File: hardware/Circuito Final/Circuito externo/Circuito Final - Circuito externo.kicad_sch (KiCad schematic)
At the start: 67 parts, among them J1 Conn_02x19_Odd_Even, J2 Conn_02x19_Odd_Even, J3 Conn_01x02, J4 Conn_01x02, J5 Conn_01x03_Pin, Q1 FDMS6681Z, Q2 FDMS6681Z, Q3 MMBT2222A, SW1 SW_SPDT, SW2 SW_DIP_x04, SW3 SW_DIP_x04, SW4 SW_DIP_x01, SW5 SW_DIP_x01, SW6 SW_DIP_x01, U1 Opamp_Quad, U2 ICL7660, U3 INA180A1

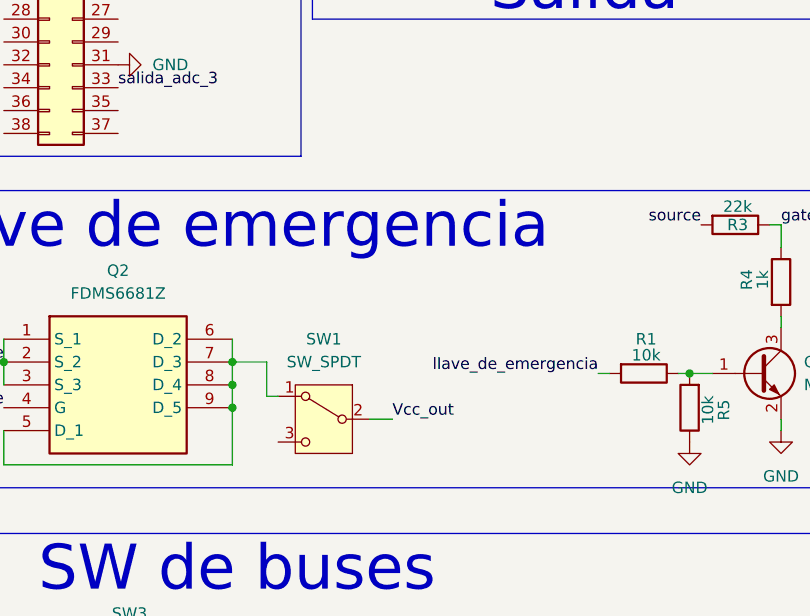
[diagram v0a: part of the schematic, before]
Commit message: agrega pull down en llave de emergencia
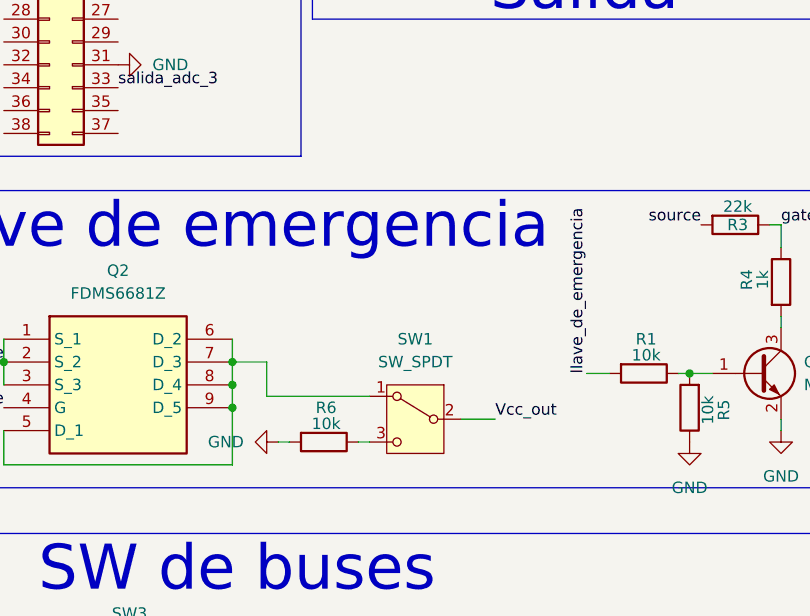
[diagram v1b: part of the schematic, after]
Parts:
- added R6: 10k, Resistor_SMD:R_1206_3216Metric_Pad1.30x1.75mm_HandSolder, symbol Device:R
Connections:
- net GND: now also R6.2
- net at SW1.3 (C): now also R6.1
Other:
- moved on the sheet: SW1
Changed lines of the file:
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@@
 	(wire
 		(pts
-			(xy 102.87 113.03) (xy 105.41 113.03)
-		)
-		(stroke
-			(width 0)
-			(type default)
-		)
-	)
-	(wire
-		(pts
 			(xy 138.43 107.95) (xy 140.97 107.95)
 		)
@@
 	(wire
 		(pts
+			(xy 93.98 115.57) (xy 92.71 115.57)
+		)
+		(stroke
+			(width 0)
+			(type default)
+		)
+	)
+	(wire
+		(pts
 			(xy 251.46 120.65) (xy 248.92 120.65)
 		)
@@
 	(wire
 		(pts
-			(xy 128.27 107.95) (xy 129.54 107.95)
+			(xy 127 107.95) (xy 129.54 107.95)
 		)
 		(stroke
@@
 	(wire
 		(pts
+			(xy 102.87 115.57) (xy 101.6 115.57)
+		)
+		(stroke
+			(width 0)
+			(type default)
+		)
+	)
+	(wire
+		(pts
 			(xy 208.28 55.88) (xy 213.36 55.88)
 		)
@@
 	(wire
 		(pts
+			(xy 113.03 113.03) (xy 116.84 113.03)
+		)
+		(stroke
+			(width 0)
+			(type default)
+		)
+	)
+	(wire
+		(pts
 			(xy 62.23 104.14) (xy 62.23 106.68)
 		)
@@
 	(wire
 		(pts
-			(xy 91.44 110.49) (xy 92.71 110.49)
+			(xy 91.44 110.49) (xy 102.87 110.49)
 		)
 		(stroke
@@
 	)
 	(label "Vcc_out"
-		(at 105.41 113.03 0)
+		(at 116.84 113.03 0)
 		(effects
 			(font
@@
 	)
 	(label "llave_de_emergencia"
-		(at 128.27 107.95 180)
+		(at 127 107.95 90)
 		(effects
 			(font
 				(size 1.27 1.27)
 			)
-			(justify right bottom)
+			(justify left bottom)
 		)
 	)
@@
 	)
 	(symbol
+		(lib_id "Device:R")
+		(at 97.79 115.57 270)
+		(unit 1)
+		(body_style 1)
+		(exclude_from_sim no)
+		(in_bom yes)
+		(on_board yes)
+		(in_pos_files yes)
+		(dnp no)
+		(property "Reference" "R6"
+			(at 98.044 111.76 90)
+			(show_name no)
+			(do_not_autoplace no)
+			(effects
+				(font
+					(size 1.27 1.27)
+				)
+			)
+		)
+		(property "Value" "10k"
+			(at 98.044 113.538 90)
+			(show_name no)
+			(do_not_autoplace no)
+			(effects
+				(font
+					(size 1.27 1.27)
+				)
+			)
+		)
+		(property "Footprint" "Resistor_SMD:R_1206_3216Metric_Pad1.30x1.75mm_HandSolder"
+			(at 97.79 113.792 90)
+			(hide yes)
+			(show_name no)
+			(do_not_autoplace no)
+			(effects
+				(font
+					(size 1.27 1.27)
+				)
+			)
+		)
+		(property "Datasheet" ""
+			(at 97.79 115.57 0)
+			(hide yes)
+			(show_name no)
+			(do_not_autoplace no)
+			(effects
+				(font
+					(size 1.27 1.27)
+				)
+			)
+		)
+		(property "Description" "Resistor"
+			(at 97.79 115.57 0)
+			(hide yes)
+			(show_name no)
+			(do_not_autoplace no)
+			(effects
+				(font
+					(size 1.27 1.27)
+				)
+			)
+		)
+		(pin "1"
+		)
+		(pin "2"
+		)
+		(instances
+			(project "Circuito Final - Circuito externo"
+				(path "/f0782466-24b0-4466-90f1-cde2f15c75b0"
+					(reference "R6")
+					(unit 1)
+				)
+			)
+		)
+	)
+	(symbol
 		(lib_id "Connector_Generic:Conn_02x07_Odd_Even")
 		(at 34.29 182.88 0)
@@
 	(symbol
 		(lib_id "Switch:SW_SPDT")
-		(at 97.79 113.03 0)
+		(at 107.95 113.03 0)
 		(mirror y)
 		(unit 1)
@@
 		(fields_autoplaced yes)
 		(property "Reference" "SW1"
-			(at 97.79 104.14 0)
+			(at 107.95 104.14 0)
 			(show_name no)
 			(do_not_autoplace no)
@@
 		)
 		(property "Value" "SW_SPDT"
-			(at 97.79 106.68 0)
+			(at 107.95 106.68 0)
 			(show_name no)
 			(do_not_autoplace no)
@@
 		)
 		(property "Footprint" "Button_Switch_THT:SW_Slide_SPDT_Straight_CK_OS102011MS2Q"
-			(at 97.79 113.03 0)
+			(at 107.95 113.03 0)
 			(hide yes)
 			(show_name no)
@@
 		)
 		(property "Datasheet" ""
-			(at 97.79 120.65 0)
+			(at 107.95 120.65 0)
 			(hide yes)
 			(show_name no)
@@
 		)
 		(property "Description" "Switch, single pole double throw"
-			(at 97.79 113.03 0)
+			(at 107.95 113.03 0)
 			(hide yes)
 			(show_name no)
@@
 					(unit 1)
 				)
+			)
+		)
+	)
+	(symbol
+		(lib_id "power:GND")
+		(at 92.71 115.57 270)
+		(unit 1)
+		(body_style 1)
+		(exclude_from_sim no)
+		(in_bom yes)
+		(on_board yes)
+		(in_pos_files yes)
+		(dnp no)
+		(fields_autoplaced yes)
+		(property "Reference" "#PWR013"
+			(at 86.36 115.57 0)
+			(hide yes)
+			(show_name no)
+			(do_not_autoplace no)
+			(effects
+				(font
+					(size 1.27 1.27)
+				)
+			)
+		)
+		(property "Value" "GND"
+			(at 88.9 115.5699 90)
+			(show_name no)
+			(do_not_autoplace no)
+			(effects
+				(font
+					(size 1.27 1.27)
+				)
+				(justify right)
+			)
+		)
+		(property "Footprint" ""
+			(at 92.71 115.57 0)
+			(hide yes)
+			(show_name no)
+			(do_not_autoplace no)
+			(effects
+				(font
+					(size 1.27 1.27)
+				)
+			)
+		)
+		(property "Datasheet" ""
+			(at 92.71 115.57 0)
+			(hide yes)
+			(show_name no)
+			(do_not_autoplace no)
+			(effects
+				(font
+					(size 1.27 1.27)
+				)
+			)
+		)
+		(property "Description" "Power symbol creates a global label with name \"GND\" , ground"
+			(at 92.71 115.57 0)
+			(hide yes)
+			(show_name no)
+			(do_not_autoplace no)
+			(effects
+				(font
+					(size 1.27 1.27)
+				)
+			)
+		)
+		(pin "1"
+		)
+		(instances
+			(project "Circuito Final - Circuito externo"
+				(path "/f0782466-24b0-4466-90f1-cde2f15c75b0"
+					(reference "#PWR013")
+					(unit 1)
+				)

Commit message: sube arreglos de la placa central
queda confirmar el switch de emergencia
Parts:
- added H1, H2, H3, H4: MountingHole, MountingHole:MountingHole_3.5mm, symbol Mechanical:MountingHole
- added TP3, TP4: TestPoint, TestPoint:TestPoint_Keystone_5005-5009_Compact, symbol Connector:TestPoint
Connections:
- net GND: now also TP3.1
- net Vcc_externo: now also TP4.1

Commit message: subida update PCB circuito externo
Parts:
- TP1, TP2: footprint TestPoint:TestPoint_Keystone_5005-5009_Compact -> Connector_PinHeader_2.54mm:PinHeader_1x01_P2.54mm_Vertical
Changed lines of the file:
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@@
 			)
 		)
-		(property "Footprint" "TestPoint:TestPoint_Keystone_5005-5009_Compact"
+		(property "Footprint" "Connector_PinHeader_2.54mm:PinHeader_1x01_P2.54mm_Vertical"
 			(at 130.81 44.45 0)
 			(hide yes)
@@
 			)
 		)
-		(property "Footprint" "TestPoint:TestPoint_Keystone_5005-5009_Compact"
+		(property "Footprint" "Connector_PinHeader_2.54mm:PinHeader_1x01_P2.54mm_Vertical"
 			(at 120.65 55.88 0)
 			(hide yes)

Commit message: listo la placa central
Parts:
- added C9: 100n, Capacitor_SMD:C_1206_3216Metric_Pad1.33x1.80mm_HandSolder, symbol Device:C_Small
- added J6: Conn_01x03_Pin, Connector_PinHeader_2.54mm:PinHeader_1x03_P2.54mm_Vertical, symbol Connector:Conn_01x03_Pin
- added R49, R50: 0, Resistor_SMD:R_1206_3216Metric_Pad1.30x1.75mm_HandSolder, symbol Device:R_US
- added U4: INA180A1, Package_TO_SOT_SMD:SOT-23-5, symbol Amplifier_Current:INA180A1
- R2: value 1m -> 20m
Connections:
- net GND: now also C9.1, R49.1, R49.2, R50.1, R50.2, U4.2 (GND)
- net Vcc_out: now also C9.2, U4.5 (V+)
- net bus_pos_salida: now also U4.4 (-)
- net medicion_corriente: now also J6.2 (Pin_2); no longer U3.1
- net shunt: now also U4.3 (+)
- new net medicion_corriente_de_carga: J6.3 (Pin_3), U4.1
- new net medicion_corriente_de_descarga: J6.1 (Pin_1), U3.1
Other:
- moved on the sheet: Bornera1, C1, C6, H1, H2, H3, H4, R2, R34, R35, R36, R37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

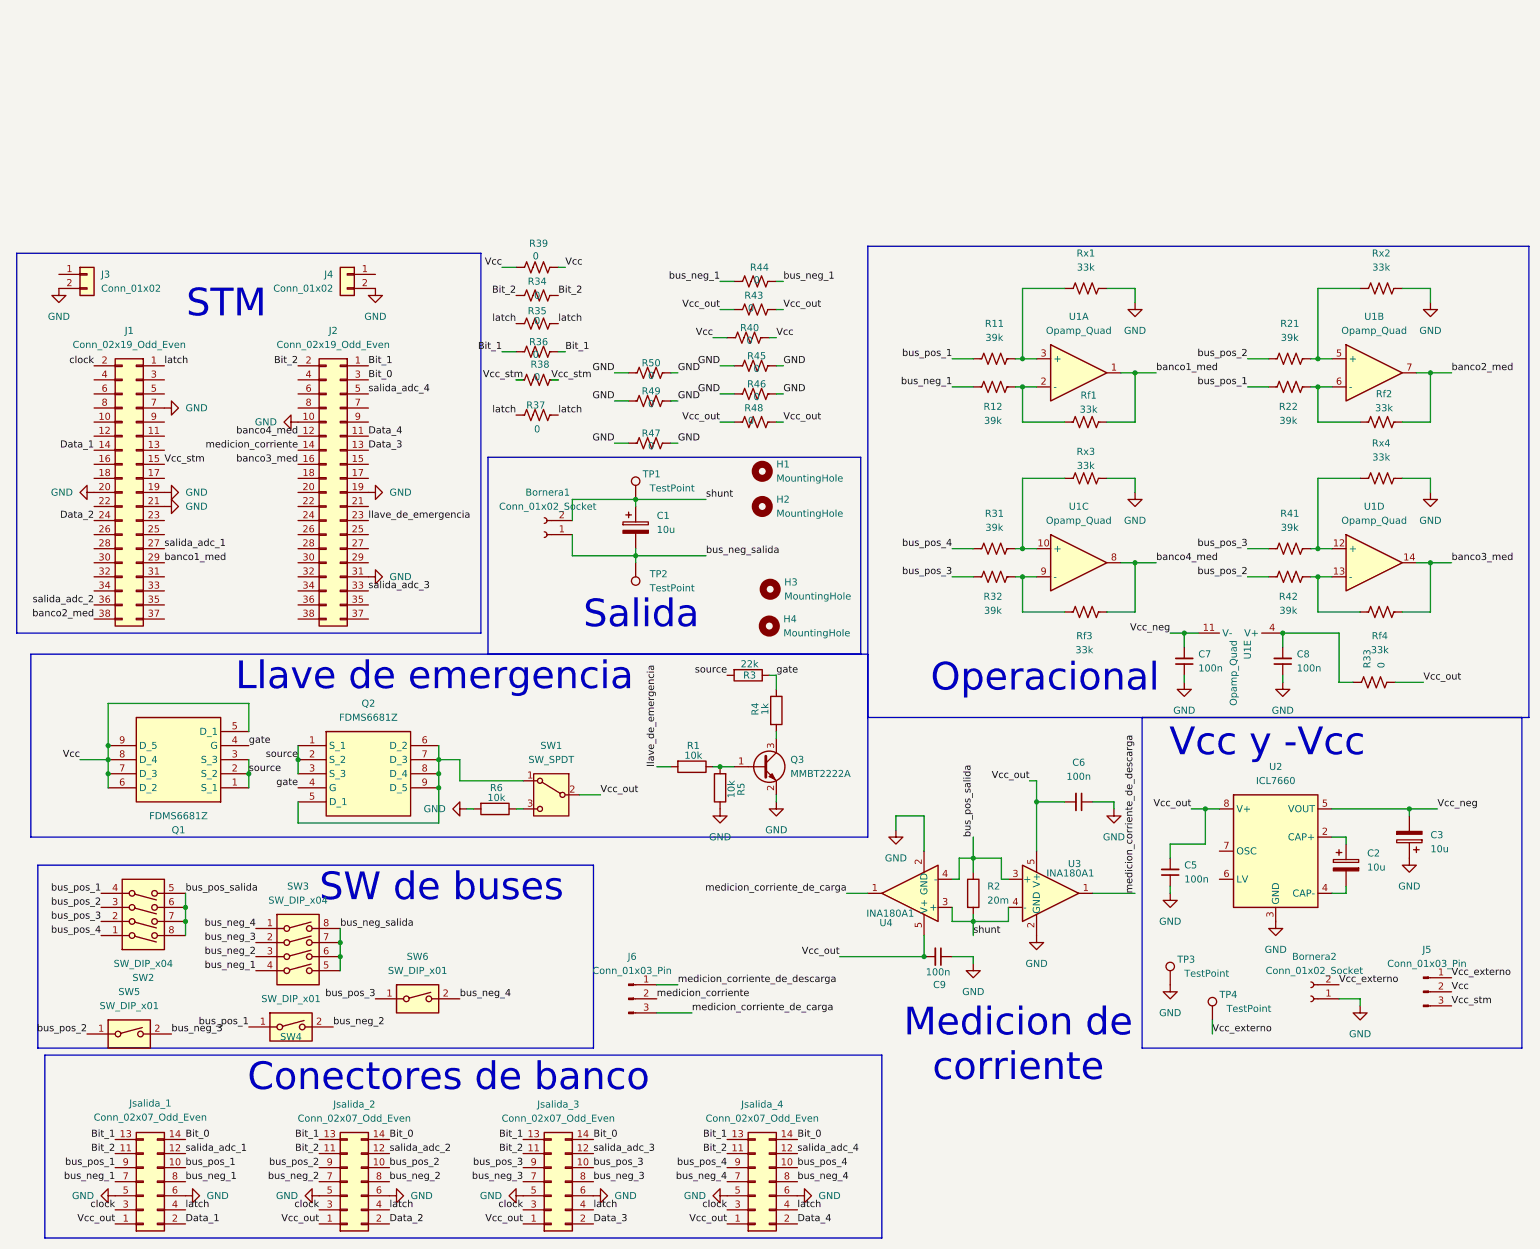
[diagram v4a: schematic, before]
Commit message: toma ambas mediciones de los ina con la stm
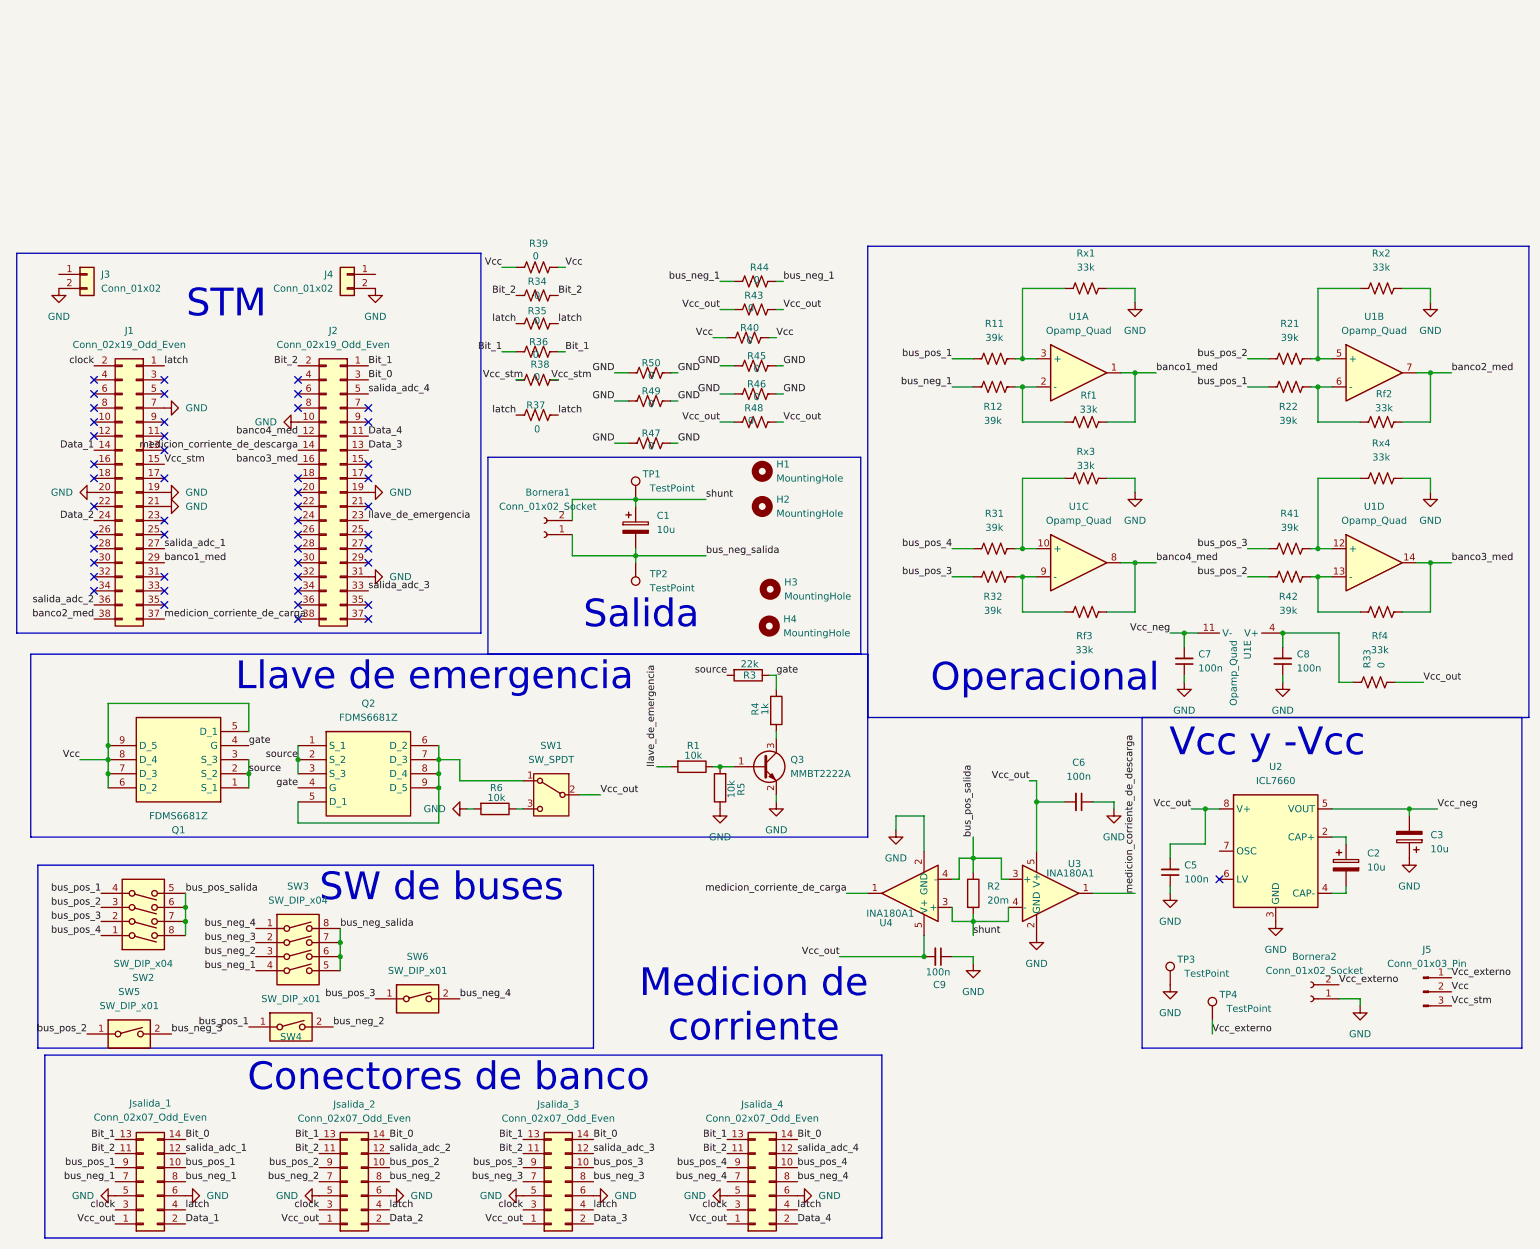
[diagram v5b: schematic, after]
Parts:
- removed J6: Conn_01x03_Pin, Connector_PinHeader_2.54mm:PinHeader_1x03_P2.54mm_Vertical, symbol Connector:Conn_01x03_Pin
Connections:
- net medicion_corriente is gone; now on net medicion_corriente_de_descarga: J2.14 (Pin_14)
- net medicion_corriente_de_carga: now also J1.37 (Pin_37)
- no-connect marks 0 -> 49

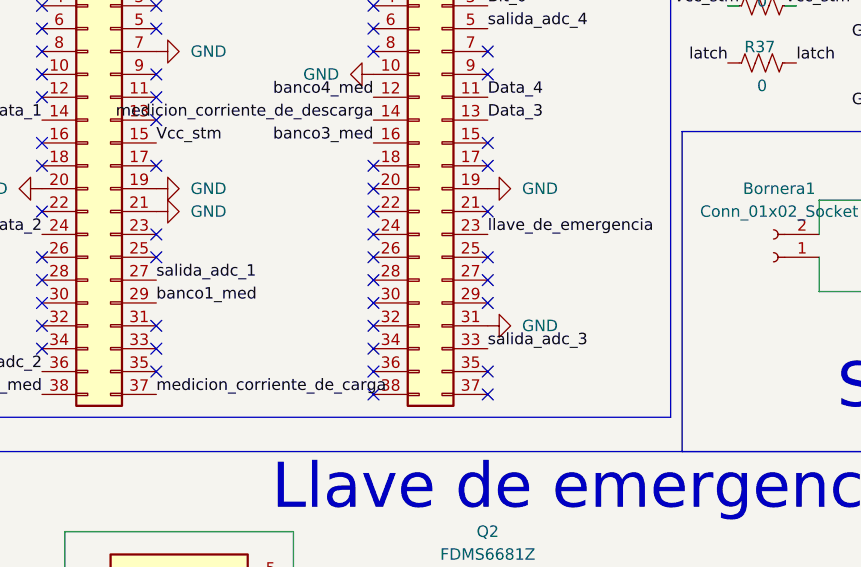
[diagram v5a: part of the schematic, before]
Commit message: acomoda un par de pistas
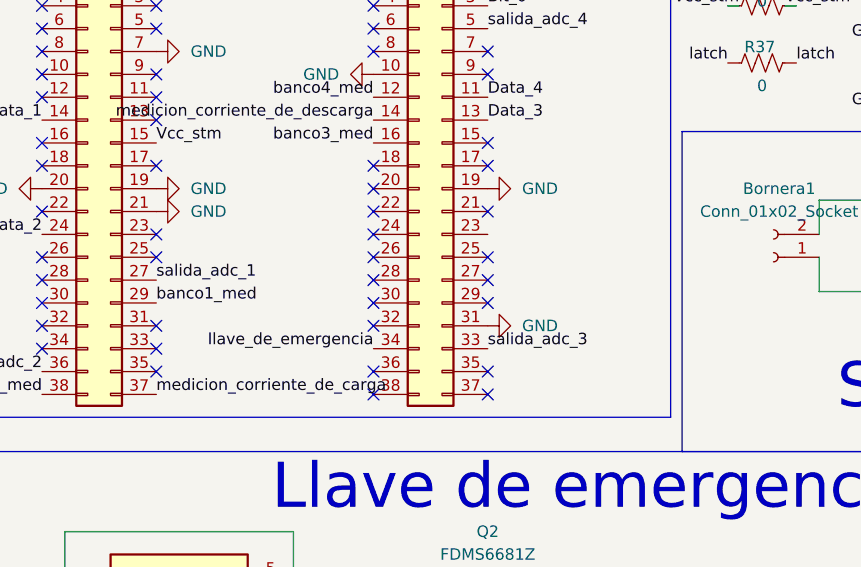
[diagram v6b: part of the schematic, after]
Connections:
- net llave_de_emergencia: now also J2.34 (Pin_34); no longer J2.23 (Pin_23)
- no-connect marks 49 -> 48
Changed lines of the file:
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@@
 	)
 	(no_connect
-		(at 62.23 76.2)
-	)
-	(no_connect
 		(at 62.23 66.04)
 	)
@@
 		)
 	)
-	(label "llave_de_emergencia"
-		(at 74.93 63.5 0)
-		(effects
-			(font
-				(size 1.27 1.27)
-			)
-			(justify left bottom)
-		)
-	)
 	(label "Bit_1"
 		(at 66.04 175.26 180)
@@
 		)
 	)
+	(label "llave_de_emergencia"
+		(at 62.23 76.2 180)
+		(effects
+			(font
+				(size 1.27 1.27)
+			)
+			(justify right bottom)
+		)
+	)

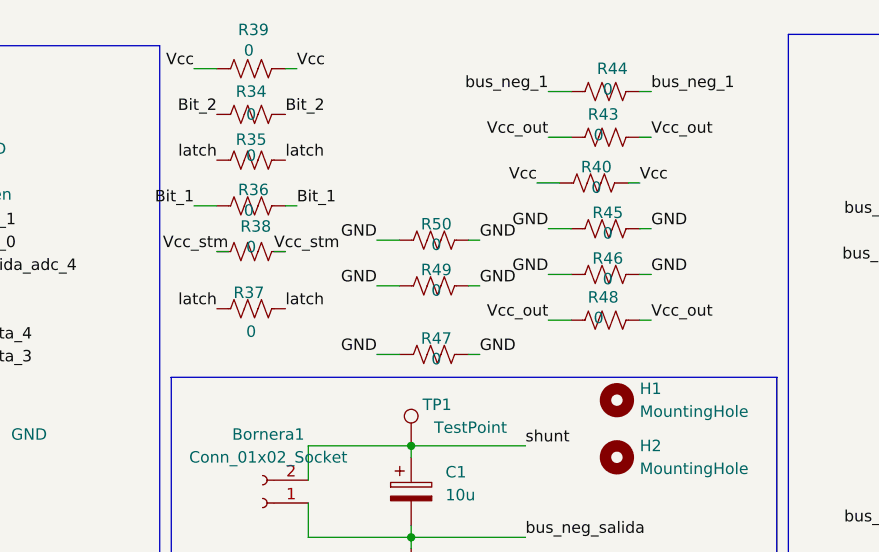
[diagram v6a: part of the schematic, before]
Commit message: conecta los gnd de la stm
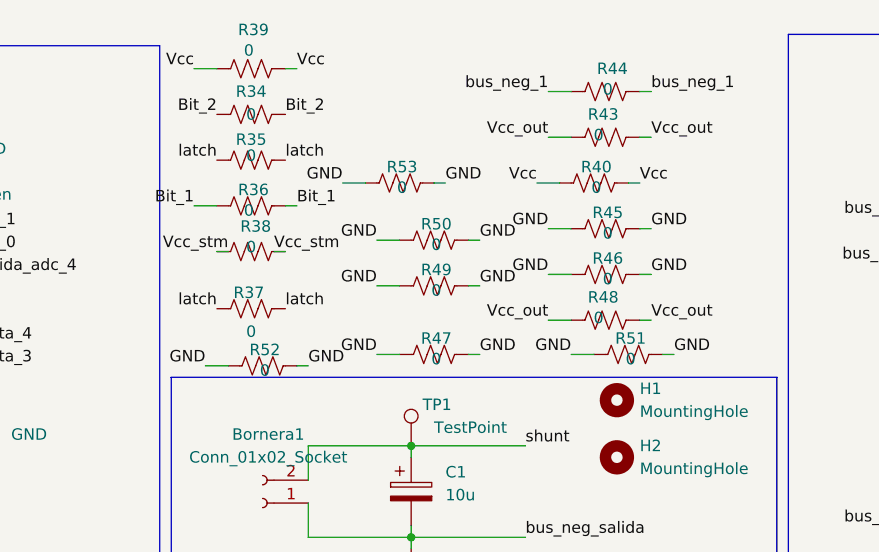
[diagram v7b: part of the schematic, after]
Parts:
- added R51, R52, R53: 0, Resistor_SMD:R_1206_3216Metric_Pad1.30x1.75mm_HandSolder, symbol Device:R_US
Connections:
- net GND: now also R51.1, R51.2, R52.1, R52.2, R53.1, R53.2
